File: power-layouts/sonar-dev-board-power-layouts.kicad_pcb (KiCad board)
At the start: 6 copper layers, 480.1 x 265.6 mm, 379 parts, among them J1001 TX_OUT_GAIN, J101 POWER, J102 DEBUG, J103 PORT1, J104 FPGA, J105 ETHERNET, J106 SYNC, J107 SONAR+, J108 SONAR+, J109 SONAR-, J110 SONAR-, J111 TRANSDUCER, J112 MOTOR, J1201 RFBT, J1202 RDAC, J401 RX_IN, J402 PREAMP, J403 BIAS_RES, J404 BIAS_RES, J405 GAIN_RES, J406 LPF_CAP, J407 VARAMP_OUT, J501 LABEL, J502 LABEL, J601 CAP, J901 OCTOSPI, Q101 DMP6023LSS-13, Q1201 SQJ974EP, Q1501 MMBT3904L, Q1502 MMBT3904L, Q1503 MMBT3904L, T101 B65655B0010X000, T701 HR641680E, U1001 SL9062D, U1002 LT1794, U1003 CSA230PASOT235, U101 LIS2DH12TR, U1101 TLV62569DBVR, U1201 LM5122MHX/NOPB, U1202 DAC53401DSGR, U1301 LM27313XMFX/NOPB, U1401 MG78L05T3, U1501 EPC23104ENGRT, U1502 EPC23104ENGRT, U1601 DRV8426RGER, U301 STM32H563AII3Q, U401 MD0100DK6-G, U402 OPA1612AIDR, U403 AD8338ACPZ-R7, U404 WS72552M-8/TR, U601 DAC53401DSGR, U602 DAC53401DSGR, U603 74LVC1G66GW,125, U701 DP83825IRMQR, U801 MIC28517T-E/PHA, U901 S27KL0642DPBHB023, X301 25MHz 8pF

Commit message: removed text of doom
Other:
- board text removed: "${REFERENCE}"
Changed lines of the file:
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@@
 		(layer "Edge.Cuts")
-	)
-	(gr_text "${REFERENCE}"
-		(at 101.7016 -73.1202 90)
-		(layer "F.Fab")
-		(effects
-			(font
-				(size 0.25 0.25)
-				(thickness 0.05)
-				(bold yes)
-			)
-		)
 	)
 	(gr_text_box "7V Boost"

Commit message: changed layout of pcbs to be more distinct
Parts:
- removed Q1502: MMBT3904L, BR_SOT:SOT-23
- R1011: moved to B.Cu
- moved TP1002 296.2 mm to (456.5, -99.4)
- moved U1003 295.5 mm to (443.6, -110.2), turned to -90 degrees
- moved TP1001 293.4 mm to (451.5, -102.9)
- moved C1007 289.6 mm to (446.4, -106.9)
- moved C1006 289.5 mm to (448.0, -106.9)
- moved R1015 289.1 mm to (443.6, -107.4), turned to 180 degrees
- moved R1014 288.2 mm to (450.4, -96.9)
- moved C1005 287.4 mm to (447.5, -108.4)
- moved J501 287.2 mm to (498.5, -104.6)
- moved J502 287.2 mm to (498.5, -95.0)
- moved R501 287.2 mm to (488.6, -87.6)
- moved R502 287.2 mm to (488.8, -89.3)
- moved TP501 287.2 mm to (486.3, -89.1)
- moved TP502 287.2 mm to (486.3, -86.8)
- moved TP503 287.2 mm to (486.3, -84.5)
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
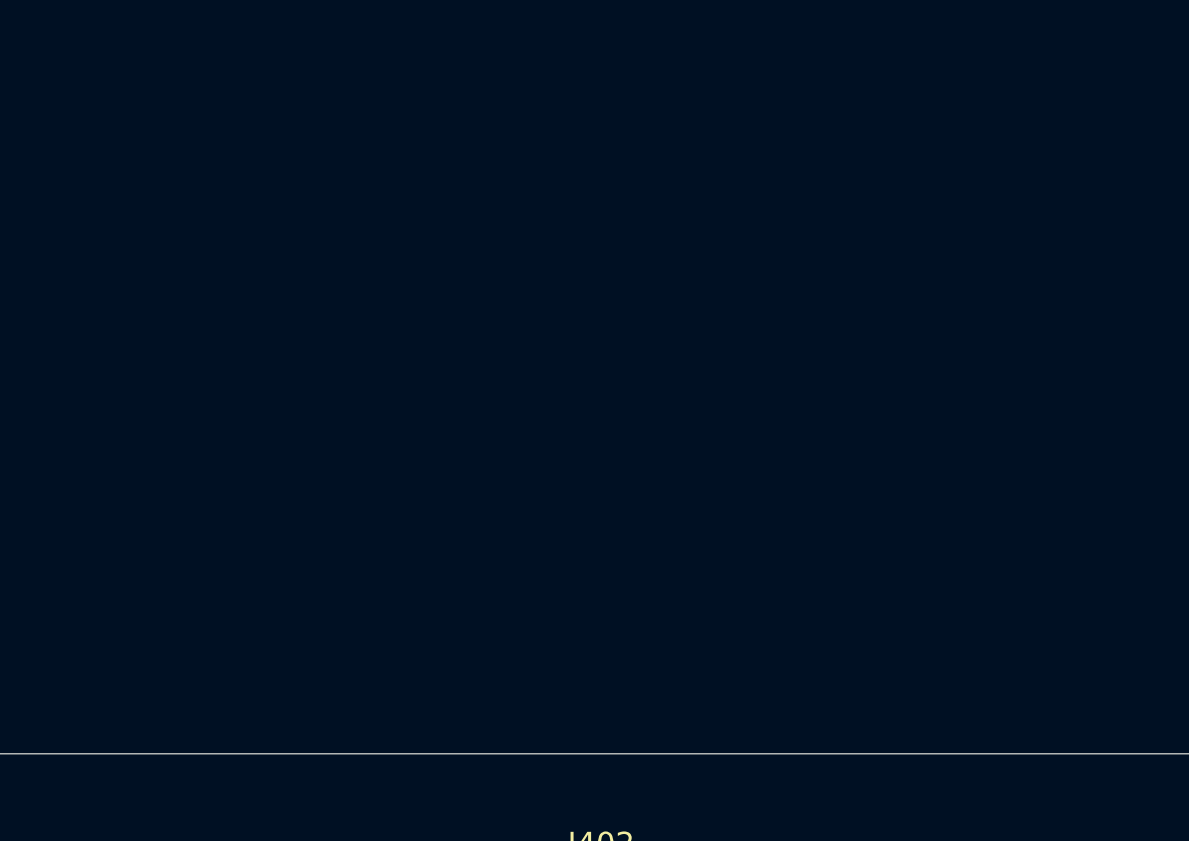
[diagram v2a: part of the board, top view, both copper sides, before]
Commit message: added RF Shield
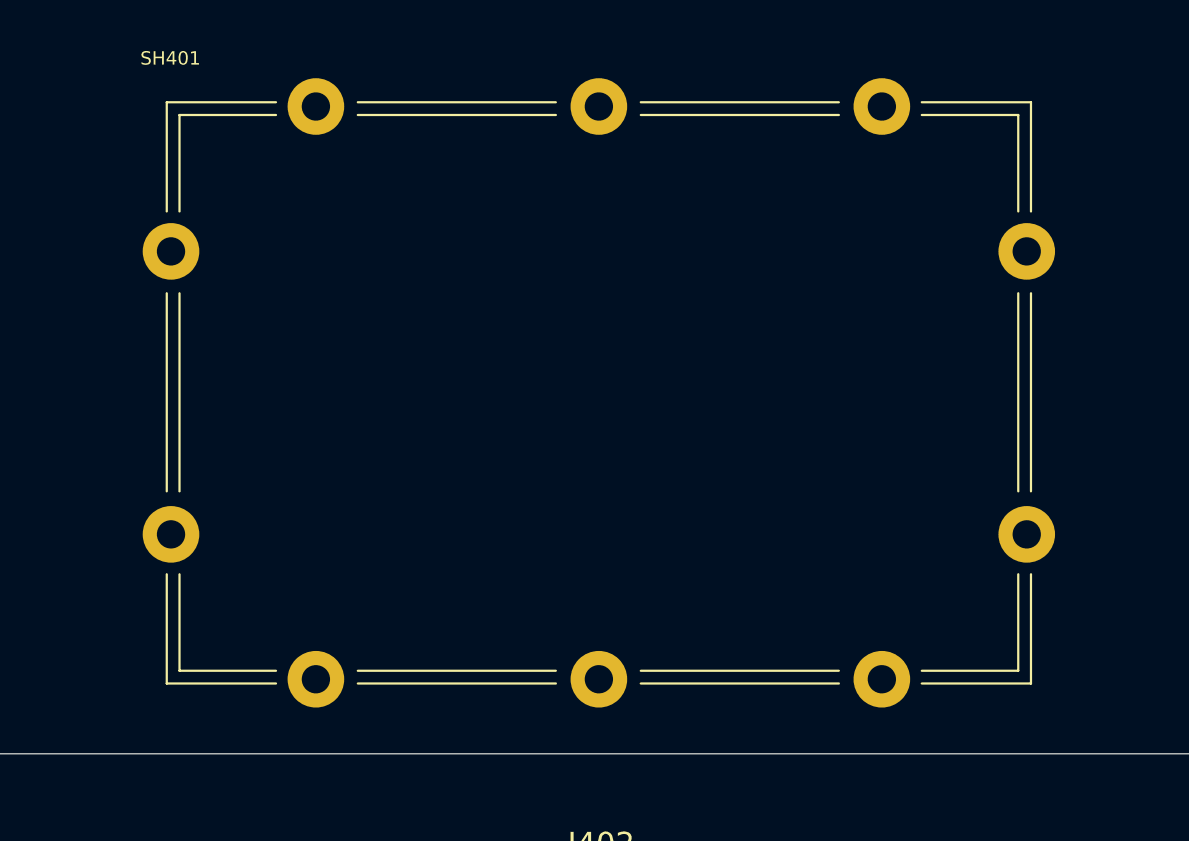
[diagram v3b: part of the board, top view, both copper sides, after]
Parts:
- added SH401: 44-CBSA-1.0X1.5X0.4, BR_Electromechanical:44-CBSA-1.0X1.5X0.4, F.Cu at (346.0, -150.3)

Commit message: Update sonar-dev-board-power-layouts.kicad_pcb
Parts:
- moved SH401 57.0 mm to (343.8, -93.4)
- moved J403 42.6 mm to (348.3, -87.5)
- moved J404 42.6 mm to (352.9, -87.5)
- moved J405 42.6 mm to (357.5, -87.5)
- moved J406 42.6 mm to (362.1, -87.5)
- moved J407 42.6 mm to (366.7, -87.5)
- moved J402 27.6 mm to (375.0, -86.5)
- moved C404 20.7 mm to (366.5, -78.0)
- moved C411 20.7 mm to (374.7, -78.5)
- moved C412 20.7 mm to (374.7, -77.5)
- moved R401 20.7 mm to (356.4, -79.5)
- moved R402 20.7 mm to (355.3, -70.5)
- moved R404 20.7 mm to (358.7, -79.5)
- moved R408 20.7 mm to (364.3, -72.0)
- moved R411 20.7 mm to (368.5, -75.5)
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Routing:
- net GND: track 13.8 -> 304.3 mm, vias 41 -> 48
- net /TX/GND_AB: track 0.00 -> 94.1 mm, vias 0 -> 4
- net /RX/VCM: track 0.00 -> 79.6 mm, vias 0 -> 1
- net /RX/PREAMP_IN+: track 0.00 -> 72.6 mm, vias 0 -> 2
- net RX_5V: track 1.13 -> 65.6 mm, vias 2 -> 7
- net /RX/PREAMP_IN-: track 0.00 -> 53.7 mm, vias 0 -> 2
- net 3V3: track 3.97 -> 55.8 mm, vias 20 -> 25
- net /RX/PREAMP_OUT-: track 0.00 -> 46.2 mm, vias 0 -> 2
- net /TX/5V_AB: track 0.00 -> 39.8 mm
- net /TX/Digital Drive/PGND: track 0.00 -> 37.4 mm
- net /TX/SIG_OUT-_AB: track 0.00 -> 36.8 mm
- net 5V: track 11.3 -> 43.6 mm, vias 48 -> 51
- net /TX/VCC_AB: track 0.00 -> 31.5 mm, vias 0 -> 2
- net Net-(J407-Pin_2): track 0.00 -> 30.8 mm, vias 0 -> 1
- net Net-(J1001-Pin_1): track 0.00 -> 28.0 mm, vias 0 -> 1
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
